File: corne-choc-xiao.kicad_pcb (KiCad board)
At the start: 2 copper layers, 111.3 x 87.7 mm, 50 parts, among them Q1 SI2302, SW10 SW_PUSH, SW11 SW_PUSH, SW12 SW_PUSH, SW14 SW_PUSH, SW15 SW_PUSH, SW16 SW_PUSH, SW17 SW_PUSH, SW18 SW_PUSH, SW19 SW_PUSH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

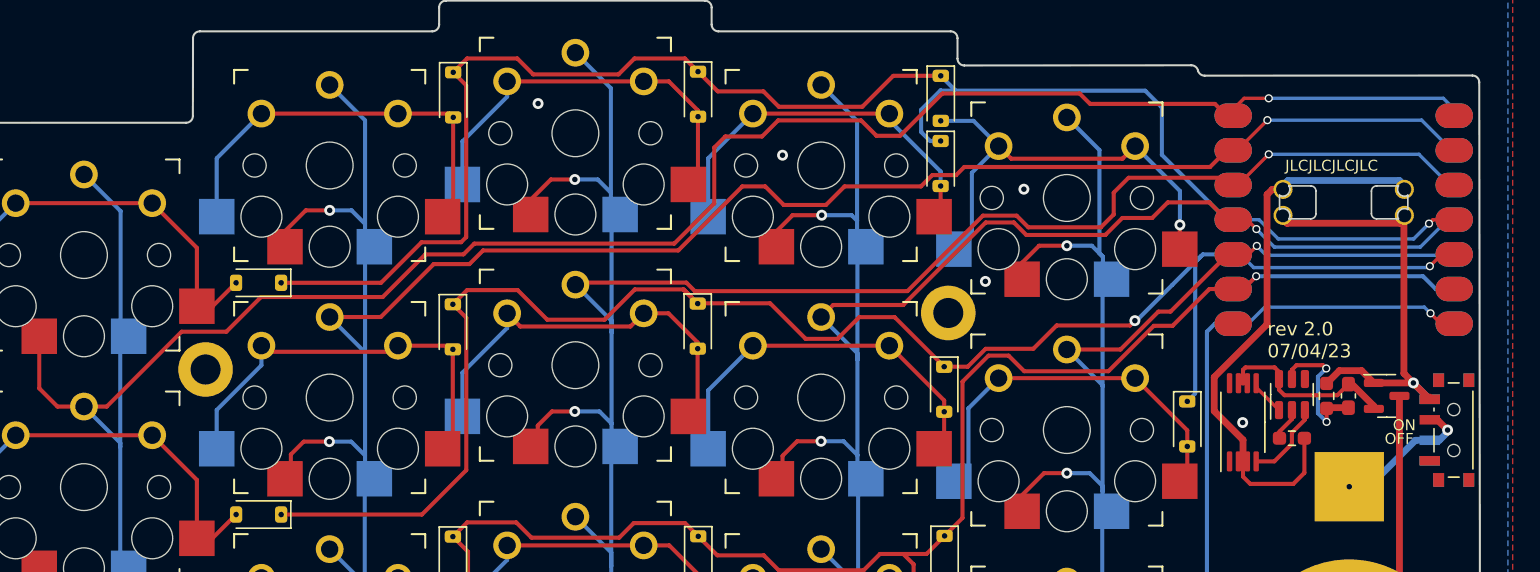
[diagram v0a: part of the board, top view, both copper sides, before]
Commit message: readded lipo terminals
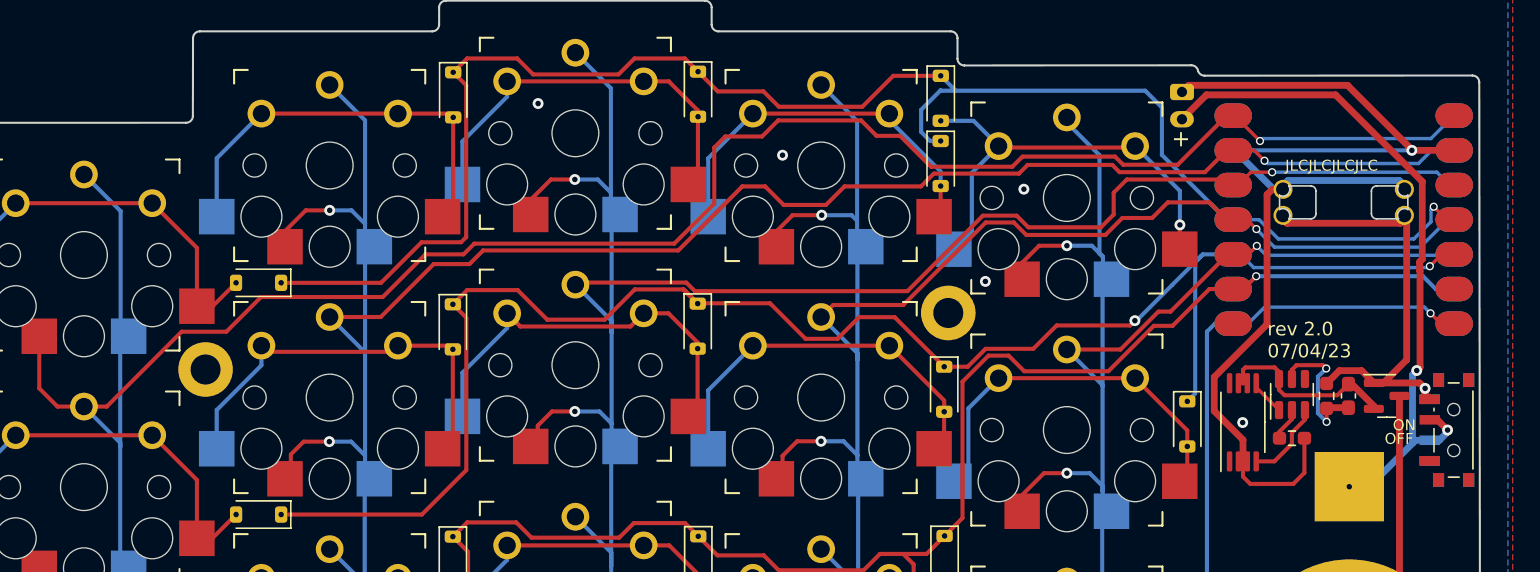
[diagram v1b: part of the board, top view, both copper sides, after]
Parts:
- added J1: LiPo, Connector_JST:JST_PH_S2B-PH-K_1x02_P2.00mm_Horizontal, B.Cu at (166.3, 53.6)
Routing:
- net GND: track 42.5 -> 87.5 mm, vias 6 -> 7
- net Net-(J1-Pin_2): track 13.2 -> 53.7 mm, vias 1 -> 2
- net col1: track 194.9 -> 196.4 mm
- net row0: track 119.0 -> 120.4 mm
- net col3: track 190.8 -> 189.6 mm
- net BAT+: track 33.0 -> 33.6 mm
- net Net-(D6-A): track 33.6 -> 32.9 mm
- net col2: track 171.4 -> 170.8 mm
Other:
- board text added: "+"
